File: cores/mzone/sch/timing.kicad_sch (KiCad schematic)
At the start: 34 parts

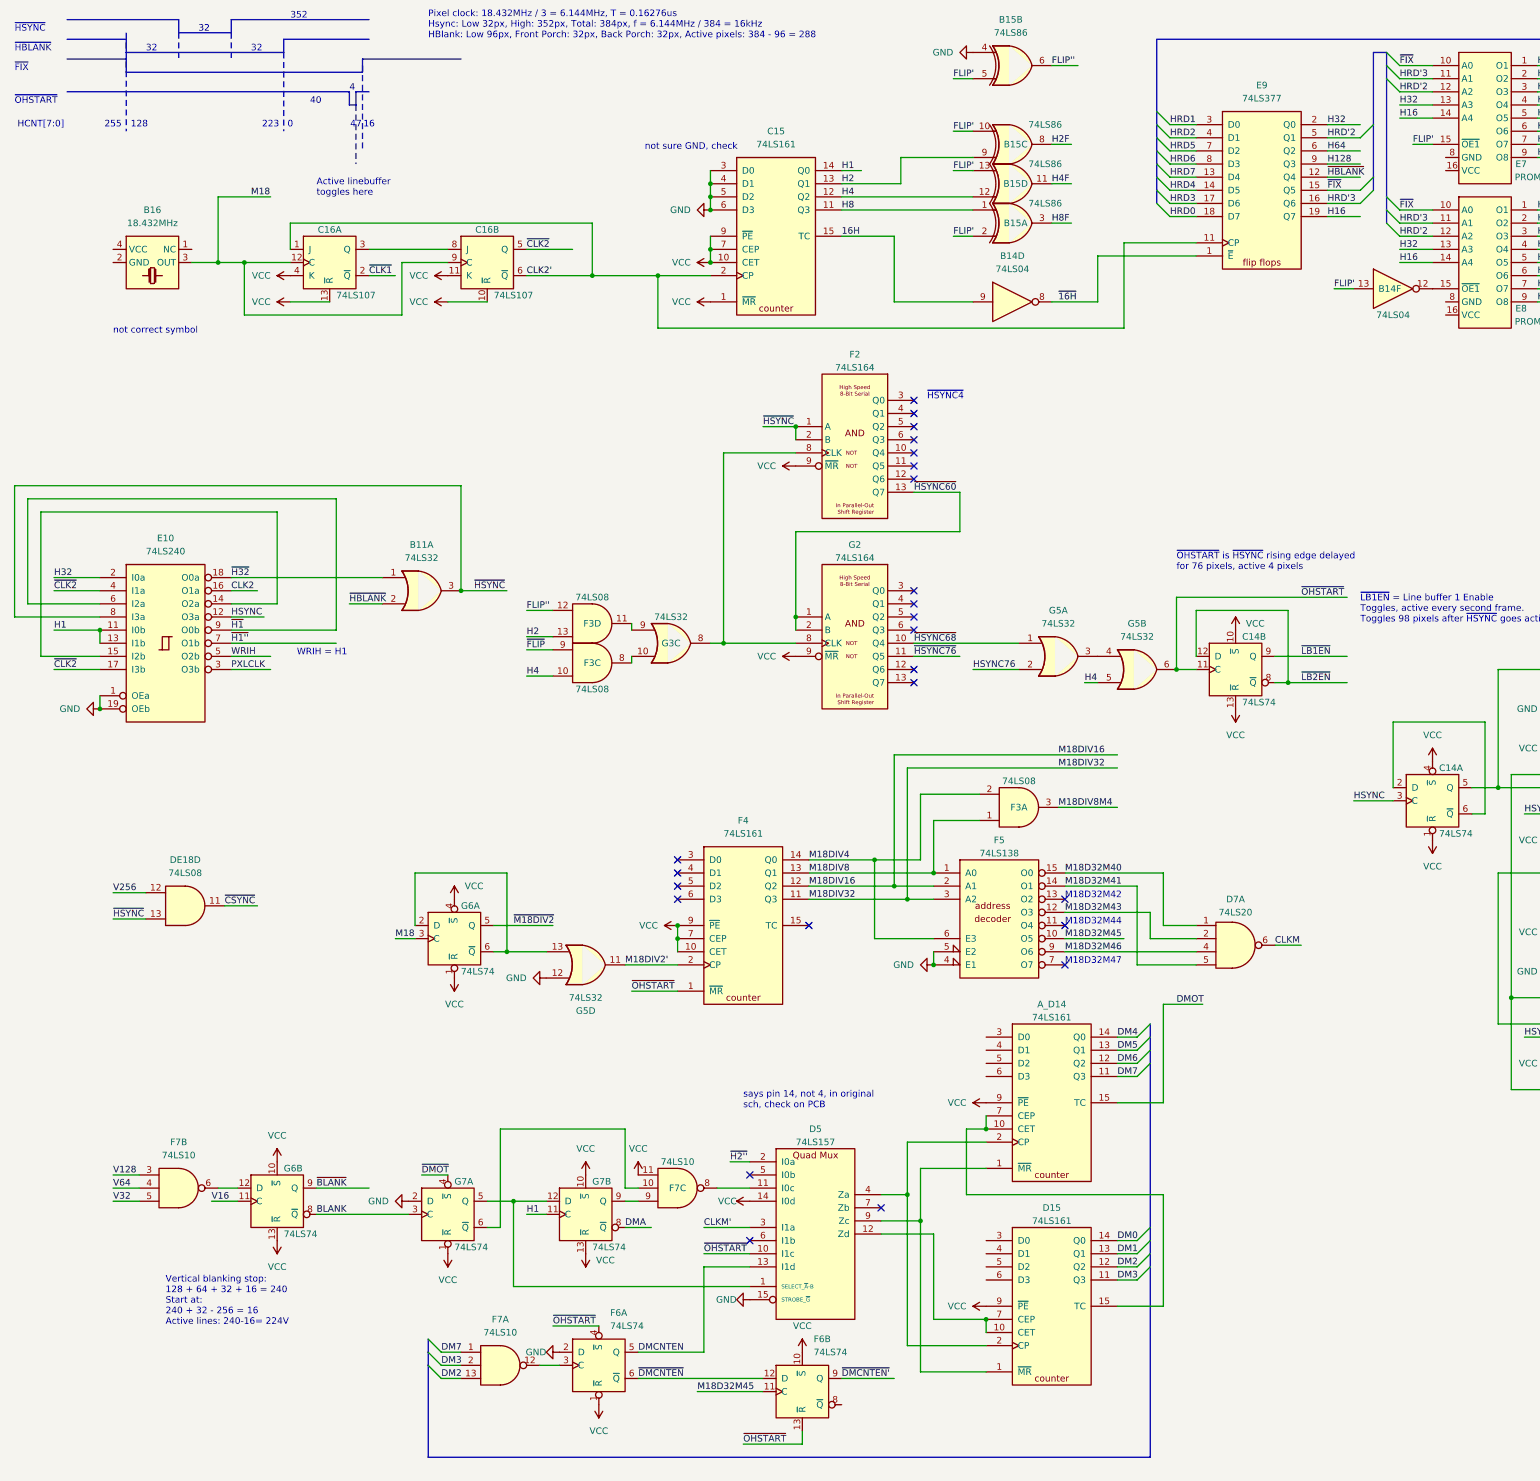
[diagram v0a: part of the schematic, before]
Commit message: mzone core
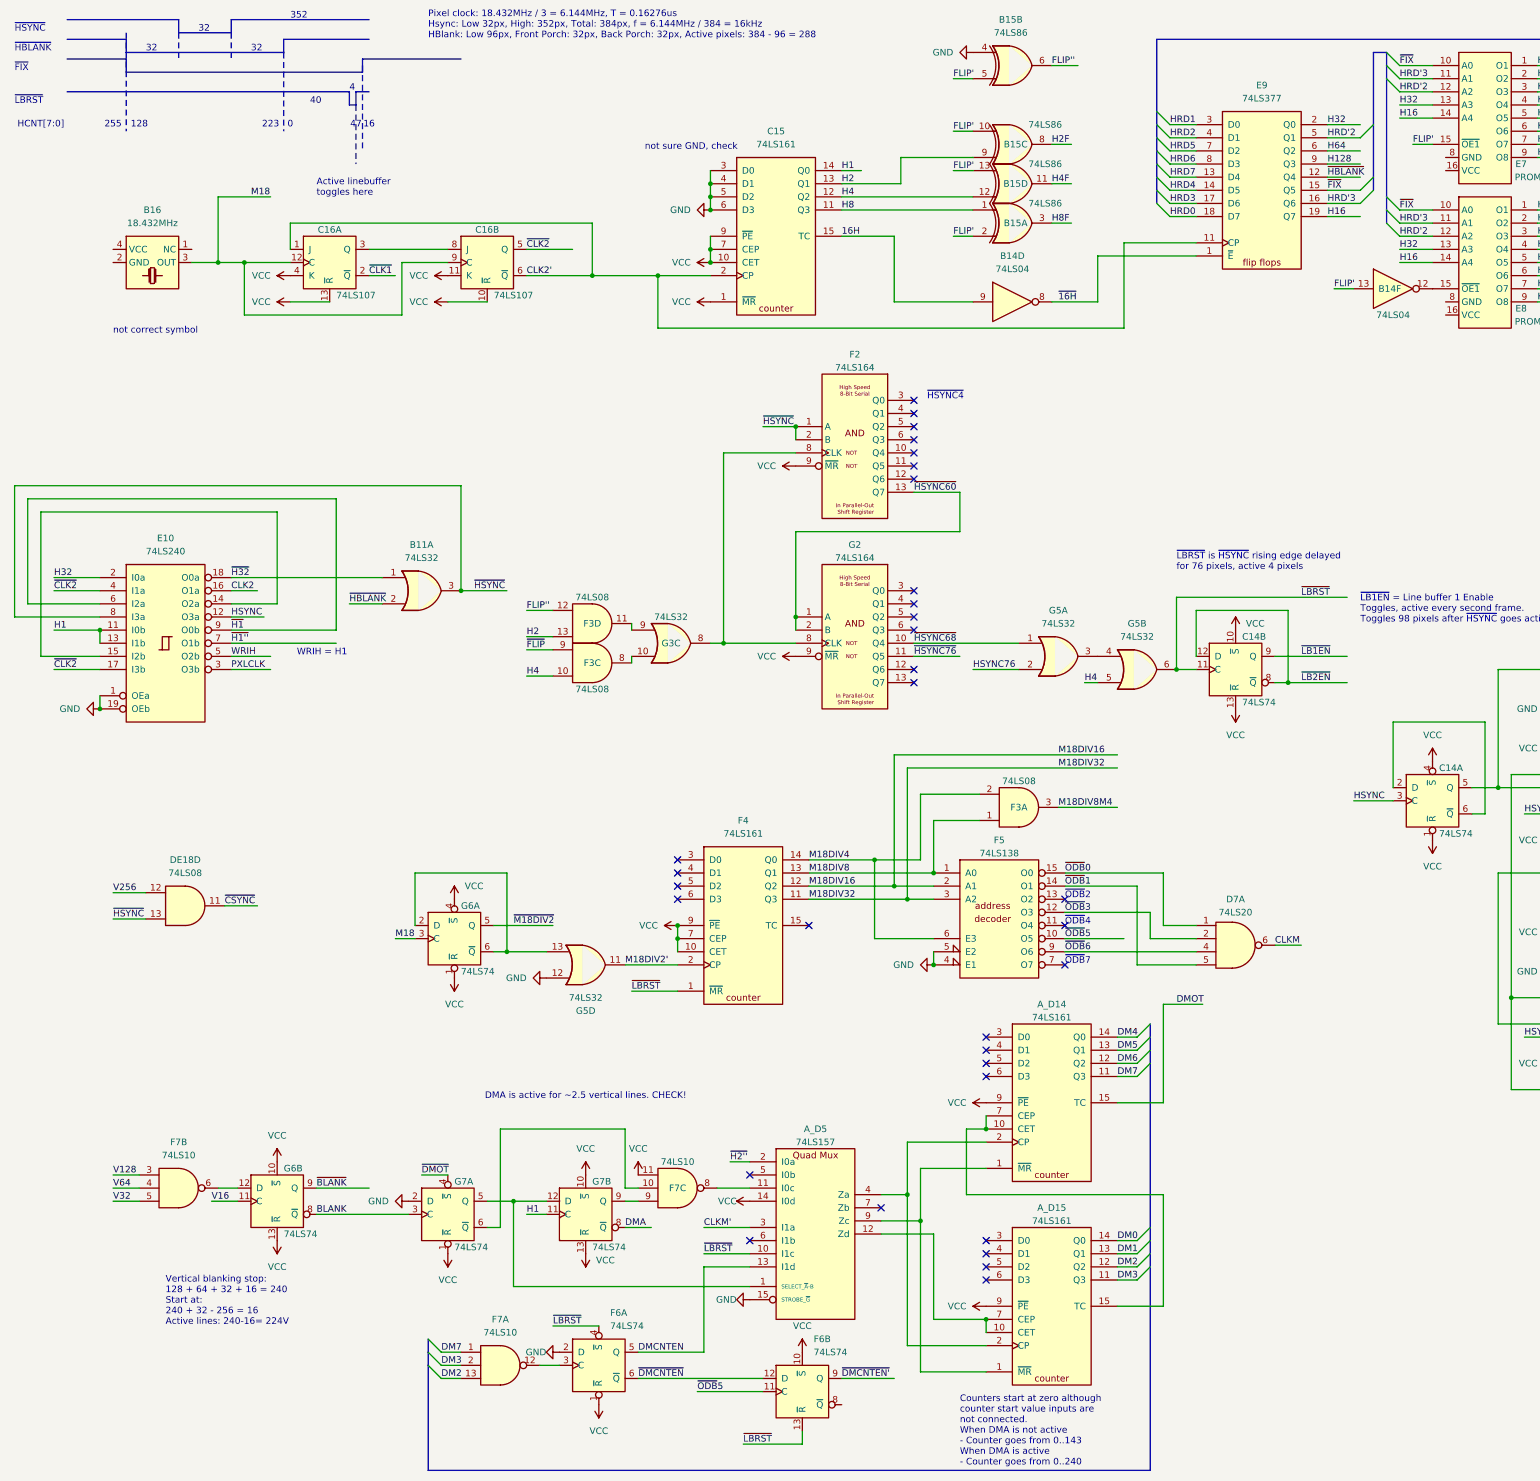
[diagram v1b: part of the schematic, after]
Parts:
- renumbered D15 to A_D15, D5 to A_D5
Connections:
- net M18D32M40 renamed ~{ODB}0
- net M18D32M41 renamed ~{ODB}1
- net M18D32M43 renamed ~{ODB}3
- net M18D32M45 renamed ~{ODB}5
- net M18D32M46 renamed ~{ODB}6
- net ~{OHSTART} renamed ~{LBRST}
- no-connect marks 26 -> 34
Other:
- note added: "Counters start at zero although counter start value inputs are not connected. When DMA is not active - Counter goes from 0..143 When DMA is active - Counter goes from 0..240"
- note added: "DMA is active for ~2.5 vertical lines. CHECK!"
- note added: "~{LBRST}"
- note added: "~{LBRST} is ~{HSYNC} rising edge delayed for 76 pixels, active 4 pixels"
- note added: "~{ODB}2"
- note added: "~{ODB}4"
- note added: "~{ODB}7"
- note removed: "M18D32M42"
- note removed: "M18D32M44"
- note removed: "M18D32M47"
- note removed: "says pin 14, not 4, in original sch, check on PCB"
- note removed: "~{OHSTART}"
- note removed: "~{OHSTART} is ~{HSYNC} rising edge delayed for 76 pixels, active 4 pixels"

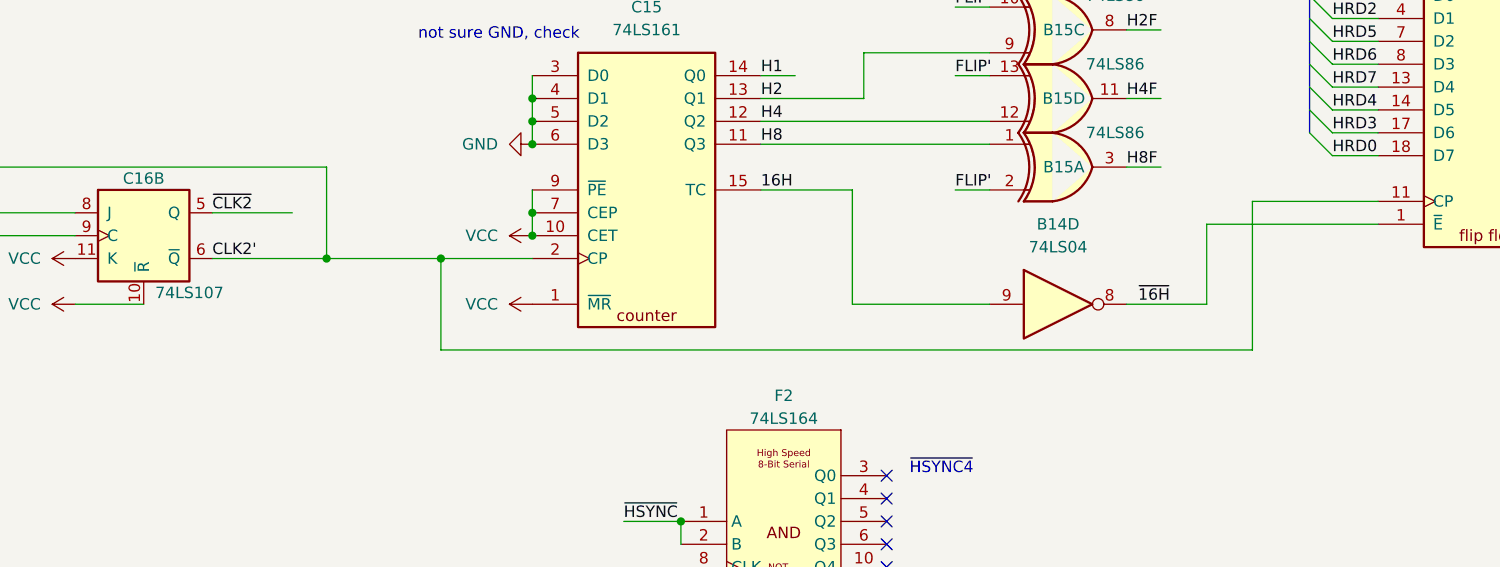
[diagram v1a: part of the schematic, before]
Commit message: mzone core
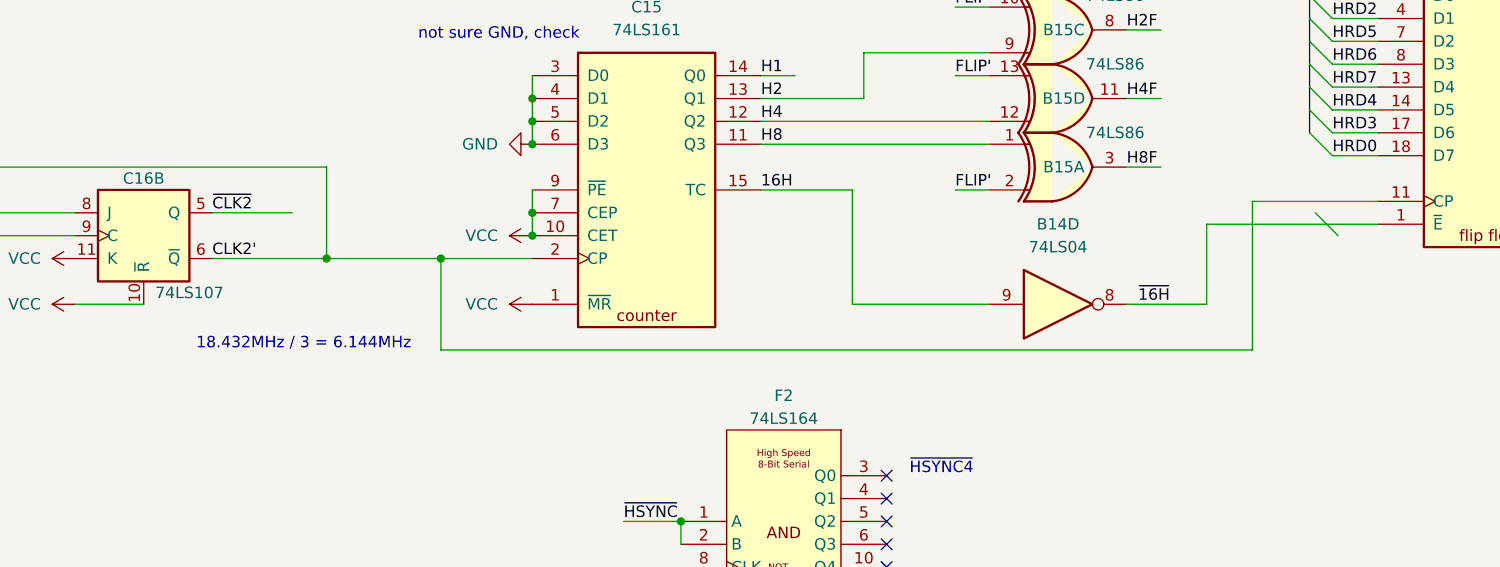
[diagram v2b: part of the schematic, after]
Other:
- note added: "18.432MHz / 3 = 6.144MHz"
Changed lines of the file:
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@@
 	)
 	(bus_entry
+		(at 247.015 60.96)
+		(size 2.54 2.54)
+		(stroke
+			(width 0)
+			(type default)
+		)
+	)
+	(bus_entry
 		(at 242.57 260.35)
 		(size 2.54 -2.54)
@@
 		(effects
 			(font
+				(size 1.27 1.27)
+			)
+		)
+	)
+	(text "18.432MHz / 3 = 6.144MHz"
+		(exclude_from_sim no)
+		(at 134.62 75.565 0)
+		(effects
+			(font

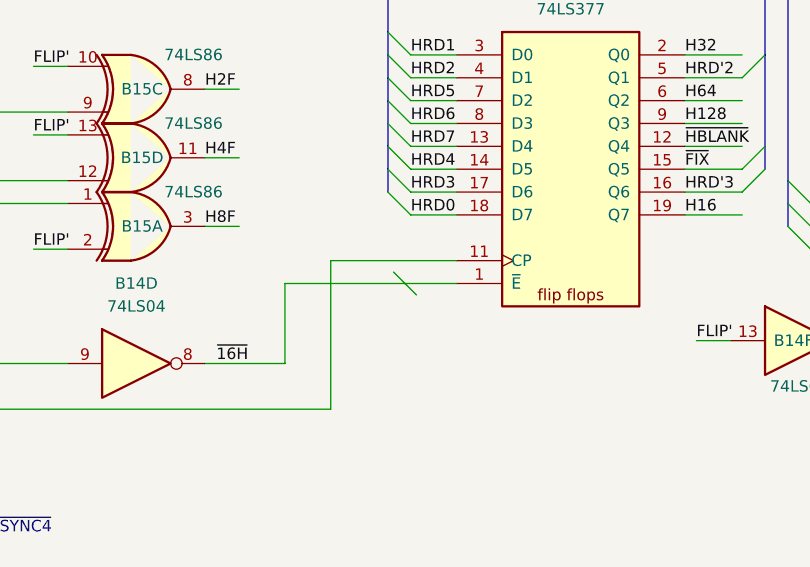
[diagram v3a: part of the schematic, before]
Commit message: mzone core
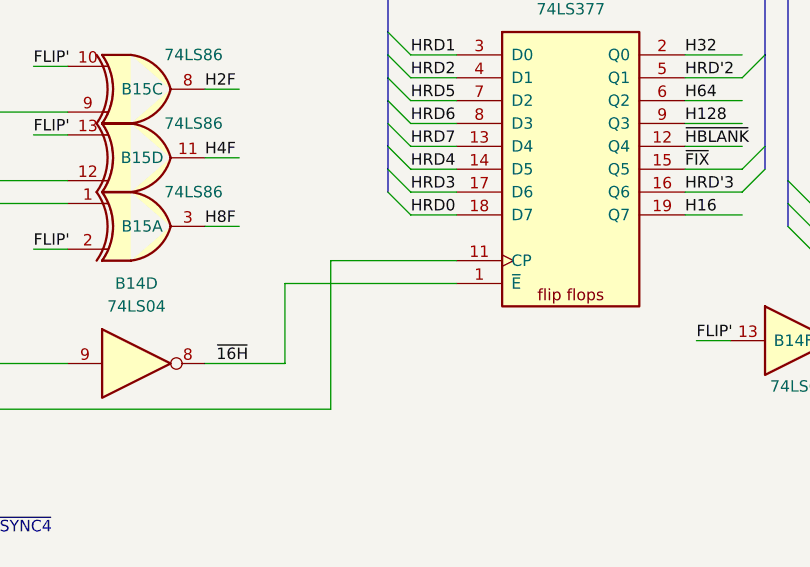
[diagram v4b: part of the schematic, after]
